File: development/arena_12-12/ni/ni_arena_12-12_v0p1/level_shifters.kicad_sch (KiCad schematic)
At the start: 191 parts, among them U10 TXB0108PW, U11 TXB0108PW, U12 TXB0108PW, U13 74LVC2G17, U14 TXB0108PW, U15 TXB0108PW, U16 TXB0108PW, U17 74LVC2G17, U18 TXB0108PW, U19 74LVC2G17, U2 TXB0108PW, U20 74LVC2G17, U21 TXB0108PW, U22 74LVC2G17, U23 74LVC2G17, U24 74LVC2G17, U25 TXB0108PW, U26 74LVC2G17, U27 74LVC2G17, U28 74LVC2G17, U29 74LVC2G17, U3 TXB0108PW, U30 TXB0108PW, U31 74LVC2G17, U32 74LVC2G17, U33 74LVC2G17, U34 74LVC2G17, U35 TXB0108PW, U36 74LVC2G17, U37 74LVC2G17, U38 74LVC2G17, U4 TXB0108PW, U5 74LVC2G17, U6 TXB0108PW, U7 TXB0108PW, U8 TXB0108PW, U9 74LVC2G17

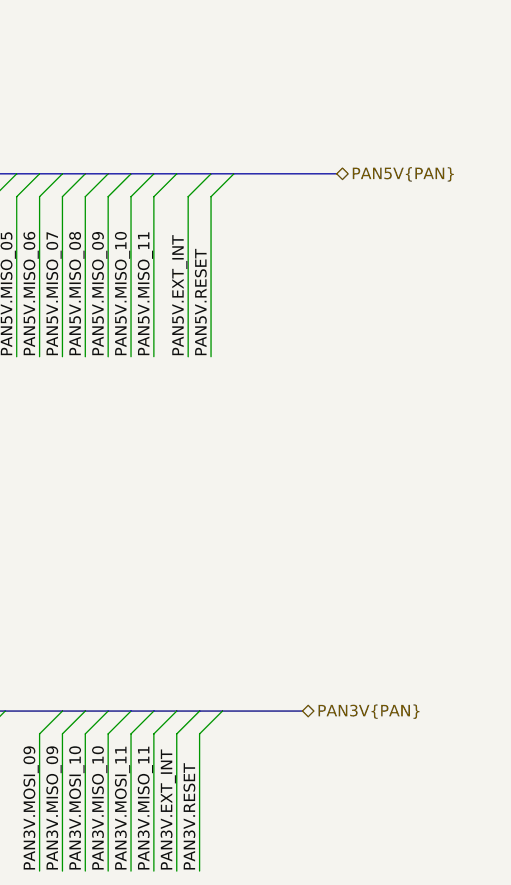
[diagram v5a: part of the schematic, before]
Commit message: Worked on NI 12-12 arena schematic.
Set up new bus definitions and started working through DRC issues.
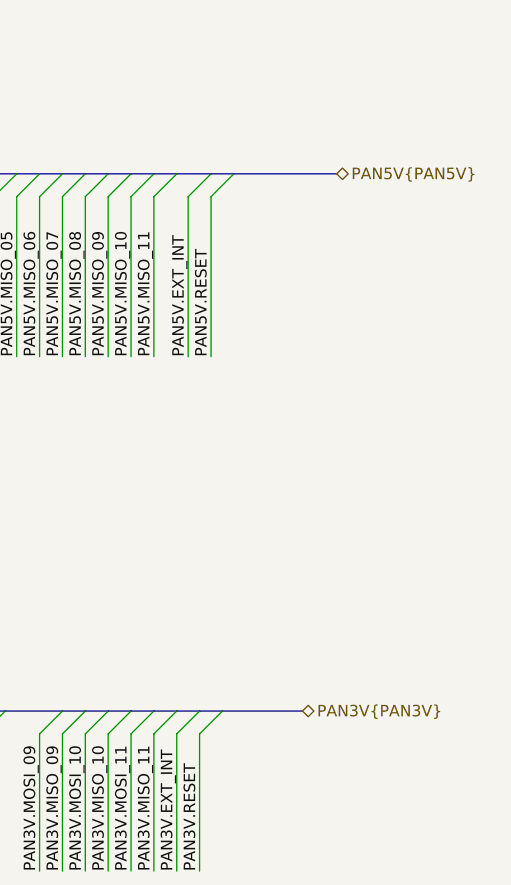
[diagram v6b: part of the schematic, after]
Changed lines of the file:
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@@
 	(generator_version "8.0")
 	(paper "User" 711.2 711.2)
+	(bus_alias "PAN5V"
+		(members "CS_0_P01" "CS_0_P02" "CS_0_P03" "CS_0_P04" "CS_0_P05" "CS_0_P06"
+			"CS_0_P07" "CS_0_P08" "CS_0_P09" "CS_0_P10" "CS_0_P11" "CS_0_P12" "CS_1_P01"
+			"CS_1_P02" "CS_1_P03" "CS_1_P04" "CS_1_P05" "CS_1_P06" "CS_1_P07" "CS_1_P08"
+			"CS_1_P09" "CS_1_P10" "CS_1_P11" "CS_1_P12" "CS_2_P01" "CS_2_P02" "CS_2_P03"
+			"CS_2_P04" "CS_2_P05" "CS_2_P06" "CS_2_P07" "CS_2_P08" "CS_2_P09" "CS_2_P10"
+			"CS_2_P11" "CS_2_P12" "CS_3_P01" "CS_3_P02" "CS_3_P03" "CS_3_P04" "CS_3_P05"
+			"CS_3_P06" "CS_3_P07" "CS_3_P08" "CS_3_P09" "CS_3_P10" "CS_3_P11" "CS_3_P12"
+			"CS_4_P01" "CS_4_P02" "CS_4_P03" "CS_4_P04" "CS_4_P05" "CS_4_P06" "CS_4_P07"
+			"CS_4_P08" "CS_4_P09" "CS_4_P10" "CS_4_P11" "CS_4_P12" "CS_5_P01" "CS_5_P02"
+			"CS_5_P03" "CS_5_P04" "CS_5_P05" "CS_5_P06" "CS_5_P07" "CS_5_P08" "CS_5_P09"
+			"CS_5_P10" "CS_5_P11" "CS_5_P12" "CS_6_P01" "CS_6_P02" "CS_6_P03" "CS_6_P04"
+			"CS_6_P05" "CS_6_P06" "CS_6_P07" "CS_6_P08" "CS_6_P09" "CS_6_P10" "CS_6_P11"
+			"CS_6_P12" "CS_7_P01" "CS_7_P02" "CS_7_P03" "CS_7_P04" "CS_7_P05" "CS_7_P06"
+			"CS_7_P07" "CS_7_P08" "CS_7_P09" "CS_7_P10" "CS_7_P11" "CS_7_P12" "SCK_0_H1"
+			"SCK_0_H2" "SCK_1_H1" "SCK_1_H2" "SCK_2_H1" "SCK_2_H2" "SCK_3_H1" "SCK_3_H2"
+			"SCK_4_H1" "SCK_4_H2" "SCK_5_H1" "SCK_5_H2" "MOSI_00" "MOSI_01" "MOSI_02"
+			"MOSI_03" "MOSI_04" "MOSI_05" "MOSI_06" "MOSI_07" "MOSI_08" "MOSI_09"
+			"MOSI_10" "MOSI_11" "MISO_00" "MISO_01" "MISO_02" "MISO_03" "MISO_04"
+			"MISO_05" "MISO_06" "MISO_07" "MISO_08" "MISO_09" "MISO_10" "MISO_11"
+			"EXT_INT" "RESET"
+		)
+	)
 	(junction
 		(at 481.33 107.95)
@@
 		)
 	)
-	(hierarchical_label "PAN3V{PAN}"
+	(hierarchical_label "PAN3V{PAN3V}"
 		(shape bidirectional)
 		(at 635 582.93 0)
@@
 		)
 	)
-	(hierarchical_label "PAN5V{PAN}"
+	(hierarchical_label "PAN5V{PAN5V}"
 		(shape bidirectional)
 		(at 638.81 523.24 0)

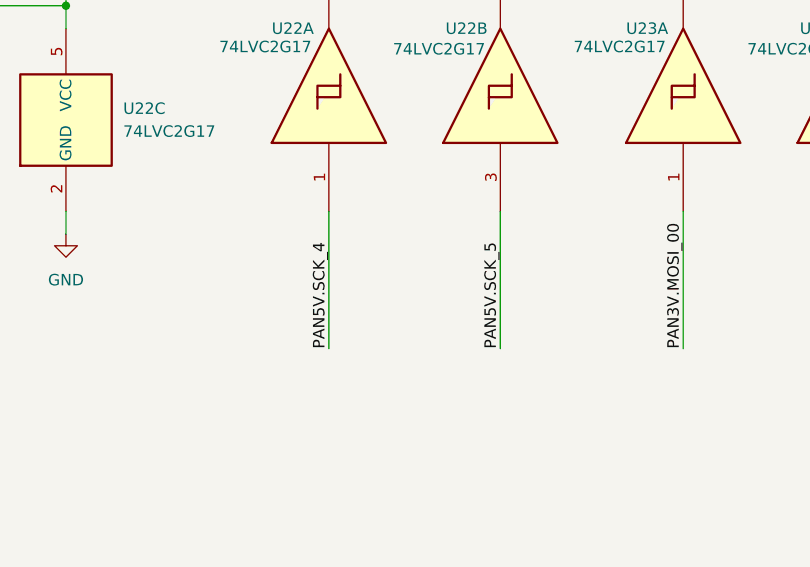
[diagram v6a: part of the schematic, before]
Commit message: ERC for NI 12-12 arena with schmitt buffers now passing.
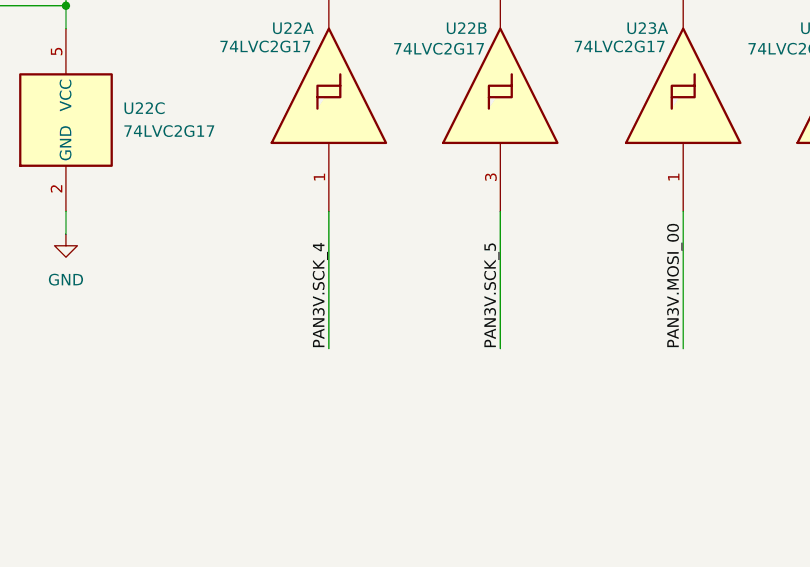
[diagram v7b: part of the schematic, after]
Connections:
- net PAN5V.SCK_4 is gone; now on net PAN3V.SCK_4: U22.1
- net PAN5V.SCK_5 is gone; now on net PAN3V.SCK_5: U22.3
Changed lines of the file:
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@@
 	)
 	(bus_entry
-		(at 546.1 585.47)
-		(size 2.54 -2.54)
-		(stroke
-			(width 0)
-			(type default)
-		)
-	)
-	(bus_entry
 		(at 381 525.78)
 		(size 2.54 -2.54)
@@
 	)
 	(bus_entry
+		(at 546.1 585.47)
+		(size 2.54 -2.54)
+		(stroke
+			(width 0)
+			(type default)
+		)
+	)
+	(bus_entry
 		(at 532.13 525.78)
 		(size 2.54 -2.54)
@@
 		)
 	)
+	(bus
+		(pts
+			(xy 548.64 582.93) (xy 551.18 582.93)
+		)
+		(stroke
+			(width 0)
+			(type default)
+		)
+	)
 	(wire
 		(pts
@@
 		)
 	)
-	(bus
-		(pts
-			(xy 548.64 582.93) (xy 551.18 582.93)
-		)
-		(stroke
-			(width 0)
-			(type default)
-		)
-	)
 	(wire
 		(pts
@@
 		)
 	)
-	(label "PAN5V.SCK_5"
-		(at 309.88 293.37 90)
-		(fields_autoplaced yes)
-		(effects
-			(font
-				(size 1.27 1.27)
-			)
-			(justify left bottom)
-		)
-	)
 	(label "PAN5V.MISO_07"
 		(at 608.33 543.56 90)
@@
 		)
 	)
-	(label "PAN5V.SCK_4"
-		(at 290.83 293.37 90)
-		(fields_autoplaced yes)
-		(effects
-			(font
-				(size 1.27 1.27)
-			)
-			(justify left bottom)
-		)
-	)
 	(label "PAN5V.CS_4_P07"
 		(at 387.35 41.91 270)
@@
 		)
 	)
+	(label "PAN3V.SCK_4"
+		(at 290.83 293.37 90)
+		(fields_autoplaced yes)
+		(effects
+			(font
+				(size 1.27 1.27)
+			)
+			(justify left bottom)
+		)
+	)
 	(label "PAN5V.CS_2_P01"
 		(at 336.55 543.56 90)
@@
 		)
 	)
+	(label "PAN3V.SCK_5"
+		(at 309.88 293.37 90)
+		(fields_autoplaced yes)
+		(effects
+			(font
+				(size 1.27 1.27)
+			)
+			(justify left bottom)
+		)
+	)

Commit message: Worked on 12-12 NI arena with schmitt buffers.
Finished footprint assignments.
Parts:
- added C107, C108, C109, C110, C111, C112, C113, C114, C115, C116, C117, C118, C119, C120, C121, C122, C123, C124, C125, C126, C127, C128, C129, C130, C131, C132, C133, C134, C135, C136, C137, C138, C139, C140: 0.1uF, Capacitor_SMD:C_0402_1005Metric, symbol Device:C_Small
- C15, C16, C17, C18, C19, C20, C21, C22, C23, C24, C25, C26, C27, C28, C29, C30, C31, C32, C33, C34: footprint (none) -> Capacitor_SMD:C_0402_1005Metric
- R100, R101, R102, R103, R104, R105, R106, R107, R108, R109, R110, R111, R112, R113, R114, R115, R116, R117, R118, R119, R120, R121, R122, R123, R124, R125, R126, R127, R128, R129, R130, R131, R132, R133, R134, R135, R136, R137, R138, R139, R140, R141, R142, R143, R144, R145, R146, R147, R148, R149, R150, R151, R152, R153, R154, R155, R156, R157, R158, R159, R160, R161, R162, R163, R164, R165, R166, R167, R168, R169, R170, R171, R172, R173, R174, R41, R42, R43, R44, R45, R46, R47, R48, R49, R50, R51, R52, R53, R54, R55, R56, R57, R58, R59, R60, R61, R62, R63, R64, R65, R66, R67, R68, R69, R70, R71, R72, R73, R74, R75, R76, R77, R78, R79, R80, R81, R82, R83, R84, R85, R86, R87, R88, R89, R90, R91, R92, R93, R94, R95, R96, R97, R98, R99: footprint (none) -> Resistor_SMD:R_0402_1005Metric
- U10: renamed from U12; footprint (none) -> Package_SO:TSSOP-20_4.4x6.5mm_P0.65mm
- U11: renamed from U14; footprint (none) -> Package_SO:TSSOP-20_4.4x6.5mm_P0.65mm
- U12: renamed from U15; footprint (none) -> Package_SO:TSSOP-20_4.4x6.5mm_P0.65mm
- U13: renamed from U16; footprint (none) -> Package_SO:TSSOP-20_4.4x6.5mm_P0.65mm
- U14: renamed from U18; footprint (none) -> Package_SO:TSSOP-20_4.4x6.5mm_P0.65mm
- U15: renamed from U21; footprint (none) -> Package_SO:TSSOP-20_4.4x6.5mm_P0.65mm
- U16: renamed from U25; footprint (none) -> Package_SO:TSSOP-20_4.4x6.5mm_P0.65mm
- U17: renamed from U30; footprint (none) -> Package_SO:TSSOP-20_4.4x6.5mm_P0.65mm
- U18: renamed from U35; footprint (none) -> Package_SO:TSSOP-20_4.4x6.5mm_P0.65mm
- U19: renamed from U5; footprint (none) -> Package_TO_SOT_SMD:SOT-23-6
- U2, U3, U4: footprint (none) -> Package_SO:TSSOP-20_4.4x6.5mm_P0.65mm
- U20: renamed from U9; footprint (none) -> Package_TO_SOT_SMD:SOT-23-6
- U21: renamed from U13; footprint (none) -> Package_TO_SOT_SMD:SOT-23-6
- U22: renamed from U17; footprint (none) -> Package_TO_SOT_SMD:SOT-23-6
- U23: renamed from U19; footprint (none) -> Package_TO_SOT_SMD:SOT-23-6
- U24: renamed from U20; footprint (none) -> Package_TO_SOT_SMD:SOT-23-6
- U25: renamed from U22; footprint (none) -> Package_TO_SOT_SMD:SOT-23-6
- U26: renamed from U23; footprint (none) -> Package_TO_SOT_SMD:SOT-23-6
- U27: renamed from U24; footprint (none) -> Package_TO_SOT_SMD:SOT-23-6
- U28: renamed from U31; footprint (none) -> Package_TO_SOT_SMD:SOT-23-6
- U29: renamed from U33; footprint (none) -> Package_TO_SOT_SMD:SOT-23-6
- U30: renamed from U32; footprint (none) -> Package_TO_SOT_SMD:SOT-23-6
- U31: renamed from U34; footprint (none) -> Package_TO_SOT_SMD:SOT-23-6
- U32: renamed from U26; footprint (none) -> Package_TO_SOT_SMD:SOT-23-6
- U33: renamed from U28; footprint (none) -> Package_TO_SOT_SMD:SOT-23-6
- U34: renamed from U27; footprint (none) -> Package_TO_SOT_SMD:SOT-23-6
- U35: renamed from U29; footprint (none) -> Package_TO_SOT_SMD:SOT-23-6
- U36, U37, U38: footprint (none) -> Package_TO_SOT_SMD:SOT-23-6
- U5: renamed from U6; footprint (none) -> Package_SO:TSSOP-20_4.4x6.5mm_P0.65mm
- U6: renamed from U7; footprint (none) -> Package_SO:TSSOP-20_4.4x6.5mm_P0.65mm
- U7: renamed from U8; footprint (none) -> Package_SO:TSSOP-20_4.4x6.5mm_P0.65mm
- U8: renamed from U10; footprint (none) -> Package_SO:TSSOP-20_4.4x6.5mm_P0.65mm
- U9: renamed from U11; footprint (none) -> Package_SO:TSSOP-20_4.4x6.5mm_P0.65mm
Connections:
- net +3.3V: now also C107.1, C109.1, C111.1, C113.1, C115.1, C117.1, C119.1, C121.1, C123.1, C125.1, C127.1, C129.1, C131.1, C133.1, C135.1, C137.1, C139.1
- net +5V: now also C108.1, C110.1, C112.1, C114.1, C116.1, C118.1, C120.1, C122.1, C124.1, C126.1, C128.1, C130.1, C132.1, C134.1, C136.1, C138.1, C140.1
- net GND: now also C107.2, C108.2, C109.2, C110.2, C111.2, C112.2, C113.2, C114.2, C115.2, C116.2, C117.2, C118.2, C119.2, C120.2, C121.2, C122.2, C123.2, C124.2, C125.2, C126.2, C127.2, C128.2, C129.2, C130.2, C131.2, C132.2, C133.2, C134.2, C135.2, C136.2, C137.2, C138.2, C139.2, C140.2
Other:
- moved on the sheet: C15, C16, C17, C18, C19, C20, C21, C22, C23, C24, C25, C26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
